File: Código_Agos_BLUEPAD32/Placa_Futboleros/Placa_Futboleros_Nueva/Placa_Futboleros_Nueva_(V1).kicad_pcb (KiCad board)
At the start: 2 copper layers, 50 x 100 mm, 16 parts, among them J1 BAT, J2 Motor_Izq_Adelante, J3 Motor_Izq_Atras, J4 Motor_Der_Adelante, J5 Motor_Der_Atras, U1 AMS1117, U2 esp32_36_pins-custom_library, U3 DRV8833, U4 DRV8833

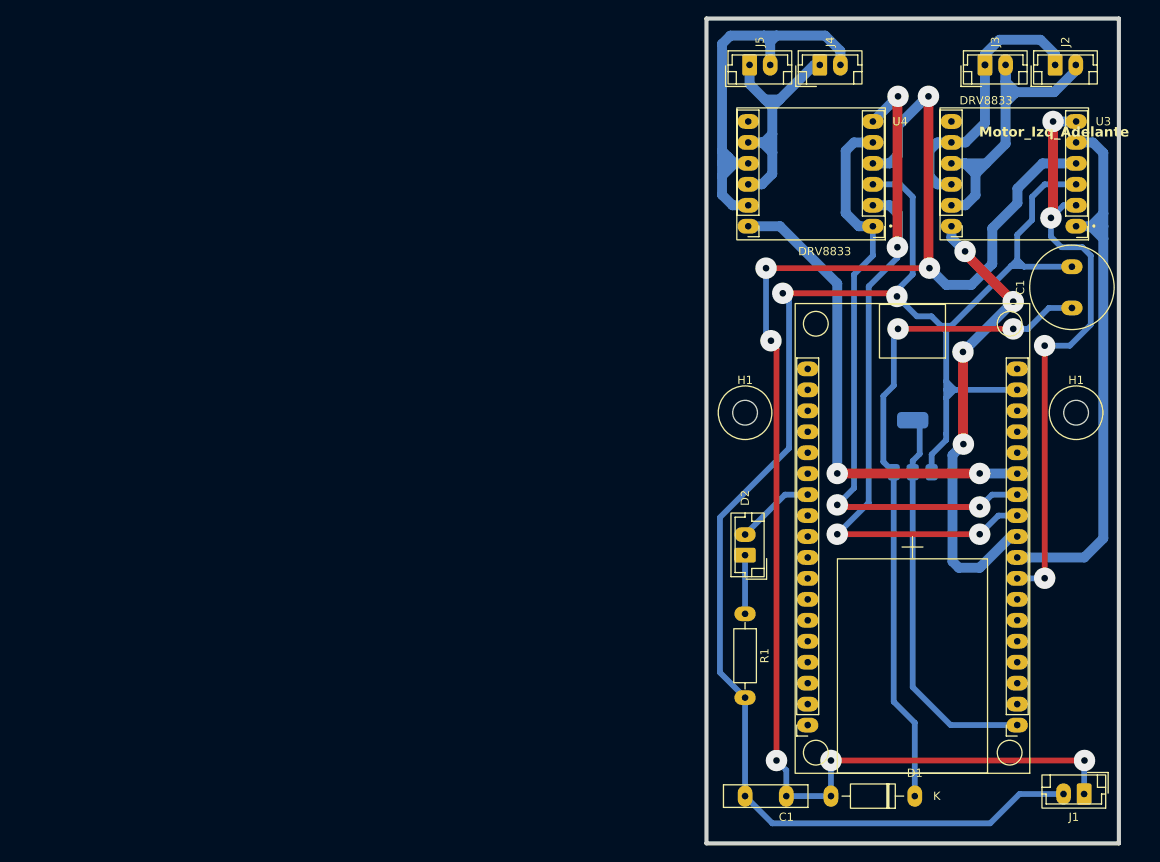
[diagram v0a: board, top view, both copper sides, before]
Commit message: Nueva Versión de Placa
Se rediseña la placa para obtener mayor espacio y disposición de elemento
además de colocar vías que sirvan tanto para puentes como placa doble faz.
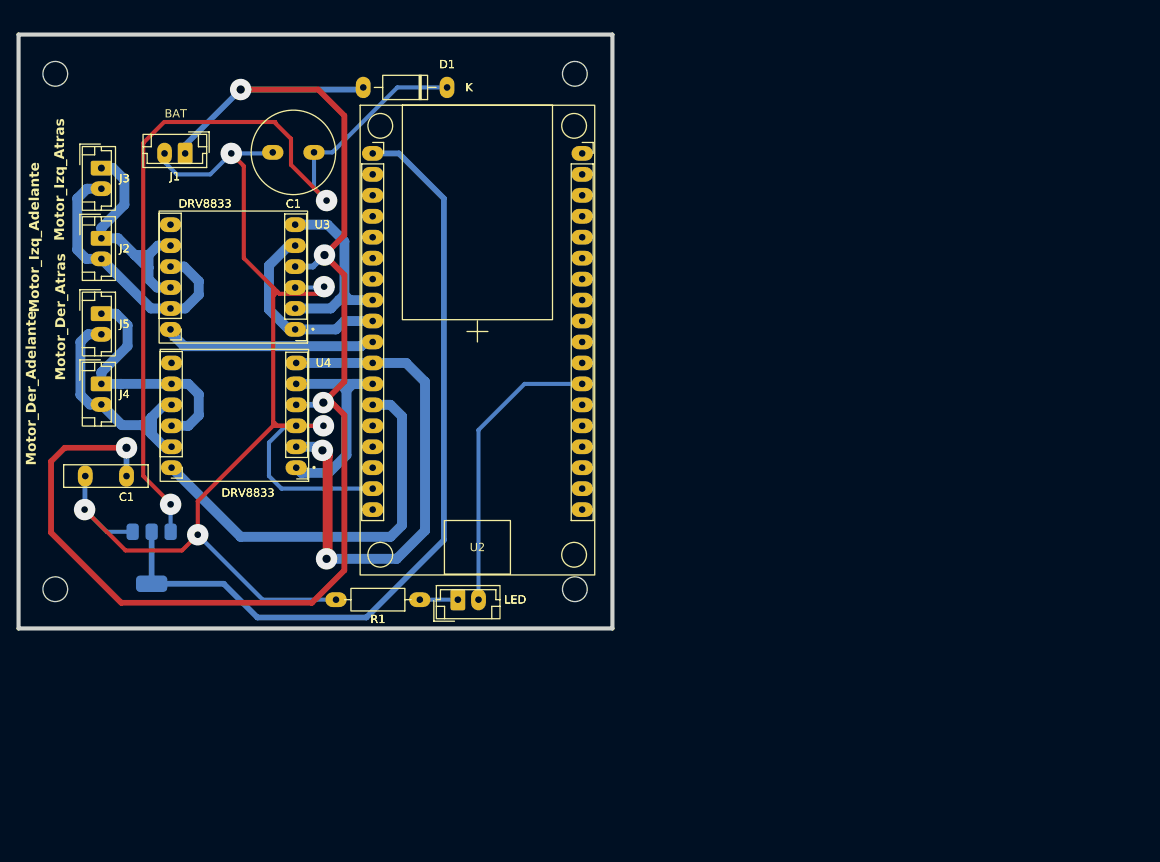
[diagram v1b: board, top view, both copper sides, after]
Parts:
- removed the H1 at (154.2, 78.2)
- removed the H1 at (194.4, 78.2)
- added H1: MountingHole, MountingHole:MountingHole_3mm, F.Cu at (70.6, 37.1)
- added H2: MountingHole, MountingHole:MountingHole_3mm, F.Cu at (70.6, 99.6)
- added H3: MountingHole, MountingHole:MountingHole_3mm, F.Cu at (133.6, 37.1)
- added H4: MountingHole, MountingHole:MountingHole_3mm, F.Cu at (133.6, 99.6)
- moved J1 133.8 mm to (86.4, 46.7)
- moved J2 117.5 mm to (76.2, 57.0), turned to -90 degrees
- moved J3 107.9 mm to (76.2, 48.5), turned to -90 degrees
- moved U2 104.4 mm to (109.1, 46.7), turned to 0 degrees
- moved D1 102.9 mm to (118.1, 38.7)
- moved U3 95.5 mm to (91.8, 51.8)
- moved J4 95.3 mm to (76.2, 74.7), turned to -90 degrees
- moved C1 93.8 mm to (102.0, 46.6), turned to 180 degrees
- moved U1 93.3 mm to (82.3, 95.8), turned to -90 degrees
- moved C1 88.9 mm to (79.2, 85.9)
- moved J5 84.2 mm to (76.2, 66.2), turned to -90 degrees
- moved U4 75.8 mm to (91.9, 68.6)
- moved R1 39.5 mm to (114.8, 100.8), turned to 180 degrees
- moved LED 35.2 mm to (119.4, 100.8), turned to 0 degrees
- renumbered D2 to LED
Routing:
- net +5V: track 47.3 -> 99.6 mm
- net GND: track 213.6 -> 164.9 mm, vias 2 -> 5
- net IN_M1B: track 72.9 -> 24.9 mm, vias 4 -> 0
- net IN_M1A: track 69.6 -> 23.5 mm
- net IN_M2A: track 73.0 -> 29.0 mm, vias 2 -> 0
- net SLEEP_M1: track 56.6 -> 25.8 mm, vias 4 -> 0
- net LED_Encendido: track 9.60 -> 35.5 mm
- net IN_M2B: track 90.0 -> 64.8 mm, vias 4 -> 2
- net Net-(D1-K): track 81.1 -> 103.5 mm
- net VCC: track 190.7 -> 169.7 mm, vias 7 -> 4
- net Net-(J4-Pin_2): track 51.2 -> 32.1 mm
- net SLEEP_M2: track 58.5 -> 49.3 mm, vias 2 -> 0
- net Net-(J2-Pin_2): track 41.4 -> 33.8 mm
- net Net-(J2-Pin_1): track 33.9 -> 29.6 mm
- net Net-(D2-K): track 7.11 -> 4.61 mm
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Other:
- board size 50 x 100 mm -> 72 x 72 mm
- board text added: "BAT"
- board text added: "C1"
- board text added: "D1"
- board text added: "DRV8833"
- board text added: "J1"
- board text added: "J2"
- board text added: "J3"
- board text added: "J4"
- board text added: "J5"
- board text added: "K"
- board text added: "LED"
- board text added: "Motor_Der_Adelante"
- board text added: "Motor_Der_Atras"
- board text added: "Motor_Izq_Atras"
- board text added: "R1"
- board text added: "U2"
- board text added: "U3"
- board text added: "U4"
